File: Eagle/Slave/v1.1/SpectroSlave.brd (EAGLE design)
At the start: 21.6 x 21.8 mm, 12 parts

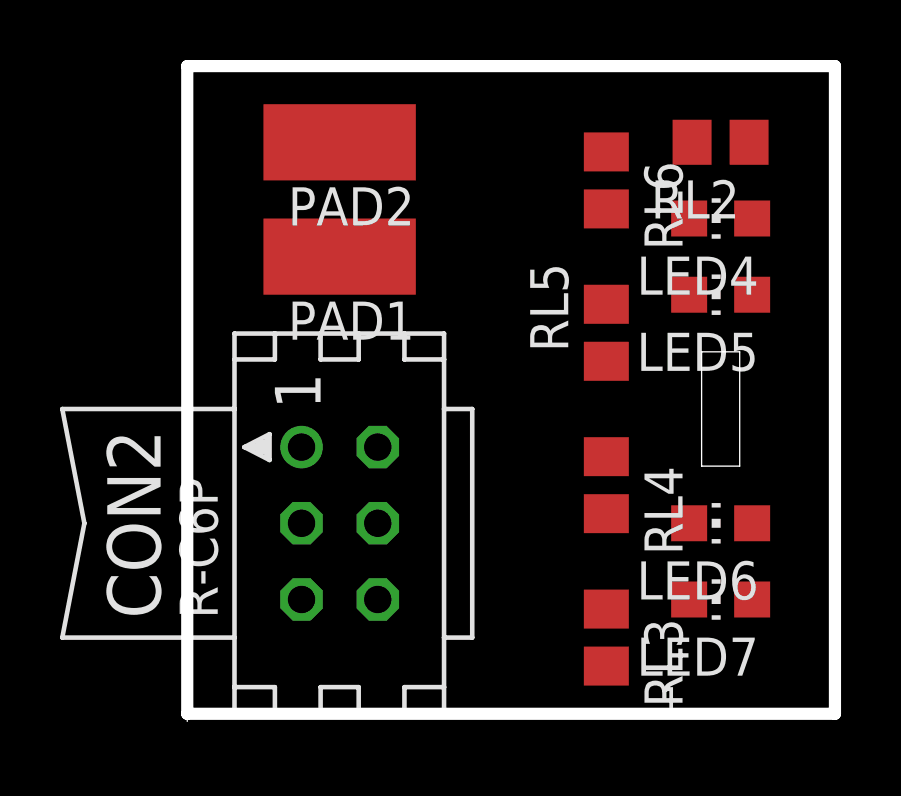
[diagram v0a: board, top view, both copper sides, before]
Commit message: Refactor the code to allow more possibilities Show linearity of the detector
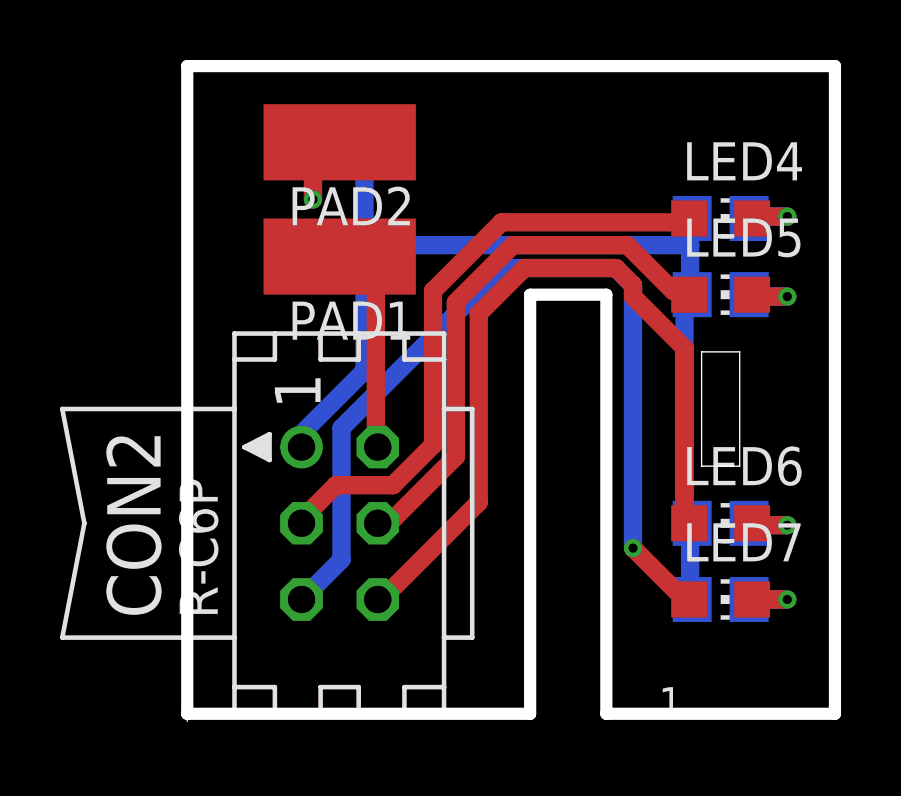
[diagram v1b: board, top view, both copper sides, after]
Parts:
- moved RL6 8.98 mm to (5.08, 19.1), flipped to the bottom, turned to 0 degrees
- moved RL3 4.02 mm to (17.8, 3.81), flipped to the bottom, turned to 0 degrees
- moved RL4 4.02 mm to (17.8, 6.35), flipped to the bottom, turned to 180 degrees
- moved RL5 4.02 mm to (17.8, 14.0), flipped to the bottom, turned to 180 degrees
- moved RL2 2.54 mm to (17.8, 16.5), flipped to the bottom, turned to 0 degrees
- turned LED4 to 270 degrees
- turned LED5 to 270 degrees
- turned LED6 to 270 degrees
- turned LED7 to 270 degrees
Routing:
- net GND: track 0.00 -> 35.2 mm
- net N$9: track 0.00 -> 29.8 mm, vias 0 -> 1
- net N$2: track 0.00 -> 25.7 mm
- net N$7: track 0.00 -> 20.2 mm
- net N$1: track 0.00 -> 17.9 mm
- net N$4: track 0.00 -> 6.91 mm
- net N$8: track 0.00 -> 4.31 mm, vias 0 -> 1
- net N$10: track 0.00 -> 2.50 mm, vias 0 -> 1
- net N$3: track 0.00 -> 2.50 mm, vias 0 -> 1
- net N$6: track 0.00 -> 2.50 mm, vias 0 -> 1
- net N$5: track 0.00 -> 2.45 mm, vias 0 -> 1
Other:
- outline, holes or cut-outs redrawn
